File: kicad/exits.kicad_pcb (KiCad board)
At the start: 2 copper layers, 38.2 x 110 mm, 66 parts, among them IC1 NJM4556AV-TE1, IC2 NJM4556AV-TE1, J1 PJ301M12, J10 Conn_01x04_Female, J11 Conn_01x04_Male, J12 Conn_02x05_Odd_Even, J13 SJ-63083A, J14 SJ-63083A, J2 PJ301M12, J3 PJ301M12, J4 PJ301M12, J5 PJ301M12, J6 PJ301M12, J7 PJ301M12, J8 Conn_01x03_Male, J9 Conn_01x03_Female, U3 LME49720, U4 LME49720

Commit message: Add files via upload
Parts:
- J10: value Conn_01x04_Female -> Conn_01x06_Female
- J11: value Conn_01x04_Male -> Conn_01x06_Male
- J12: value Conn_02x05_Odd_Even -> Euro power header
- J8: value Conn_01x03_Male -> Conn_01x04_Male
- J9: value Conn_01x03_Female -> Conn_01x04_Female
- R11, R4: value 439k -> 442k
- R12, R3: value 103k -> 102k
- R13, R2: value 1M67 -> 1M69
- R7, R8: value 141k -> 140k
- RV1: value R_POT_Dual_Separate -> 50k A
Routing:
- net Net-(J9-Pad4): track 65.7 -> 65.1 mm
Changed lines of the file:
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@@
       (effects (font (size 1 1) (thickness 0.15)))
     )
-    (fp_text value "Conn_01x03_Male" (at 0 9.95) (layer "F.Fab")
+    (fp_text value "Conn_01x04_Male" (at 0 9.95) (layer "F.Fab")
       (effects (font (size 1 1) (thickness 0.15)))
     )
@@
       (effects (font (size 1 1) (thickness 0.15)))
     )
-    (fp_text value "Conn_01x04_Male" (at 0 15.03 90) (layer "F.Fab")
+    (fp_text value "Conn_01x06_Male" (at 0 15.03 90) (layer "F.Fab")
       (effects (font (size 1 1) (thickness 0.15)))
     )
@@
       (effects (font (size 1 1) (thickness 0.15)))
     )
-    (fp_text value "R_POT_Dual_Separate" (at 3.5 2.25 180) (layer "F.Fab") hide
+    (fp_text value "50k A" (at 3.5 2.25 180) (layer "F.Fab") hide
       (effects (font (size 1 1) (thickness 0.15)))
     )
@@
     (property "Sheetname" "")
     (attr through_hole)
-    (fp_text reference "J14" (at -4.325 -9.135 90) (layer "F.SilkS")
+    (fp_text reference "J14" (at -4.7 -6.3 90) (layer "F.SilkS")
       (effects (font (size 1 1) (thickness 0.15)))
     )
@@
     (property "Sheetname" "")
     (attr through_hole)
-    (fp_text reference "J13" (at -4.325 -9.135 90) (layer "F.SilkS")
+    (fp_text reference "J13" (at -5.4 -6.9 90) (layer "F.SilkS")
       (effects (font (size 1 1) (thickness 0.15)))
     )
@@
       (effects (font (size 0.6 0.6) (thickness 0.1)) (justify mirror))
     )
-    (fp_text value "1M67" (at 0 -1.27) (layer "B.Fab")
+    (fp_text value "1M69" (at 0 -1.27) (layer "B.Fab")
       (effects (font (size 0.6 0.6) (thickness 0.1)) (justify mirror))
     )
@@
       (effects (font (size 0.6 0.6) (thickness 0.1)) (justify mirror))
     )
-    (fp_text value "103k" (at 0 -1.27) (layer "B.Fab")
+    (fp_text value "102k" (at 0 -1.27) (layer "B.Fab")
       (effects (font (size 0.6 0.6) (thickness 0.1)) (justify mirror))
     )
@@
       (effects (font (size 0.6 0.6) (thickness 0.1)) (justify mirror))
     )
-    (fp_text value "439k" (at 0 -1.27) (layer "B.Fab")
+    (fp_text value "442k" (at 0 -1.27) (layer "B.Fab")
       (effects (font (size 0.6 0.6) (thickness 0.1)) (justify mirror))
     )
@@
       (effects (font (size 0.6 0.6) (thickness 0.1)) (justify mirror))
     )
-    (fp_text value "141k" (at 0 -1.27) (layer "B.Fab")
+    (fp_text value "140k" (at 0 -1.27) (layer "B.Fab")
       (effects (font (size 0.6 0.6) (thickness 0.1)) (justify mirror))
     )
@@
       (effects (font (size 0.6 0.6) (thickness 0.1)) (justify mirror))
     )
-    (fp_text value "141k" (at 0 -1.27) (layer "B.Fab")
+    (fp_text value "140k" (at 0 -1.27) (layer "B.Fab")
       (effects (font (size 0.6 0.6) (thickness 0.1)) (justify mirror))
     )
@@
       (effects (font (size 0.6 0.6) (thickness 0.1)) (justify mirror))
     )
-    (fp_text value "439k" (at 0 -1.27) (layer "B.Fab")
+    (fp_text value "442k" (at 0 -1.27) (layer "B.Fab")
       (effects (font (size 0.6 0.6) (thickness 0.1)) (justify mirror))
     )
@@
       (effects (font (size 0.6 0.6) (thickness 0.1)) (justify mirror))
     )
-    (fp_text value "103k" (at 0 -1.27) (layer "B.Fab")
+    (fp_text value "102k" (at 0 -1.27) (layer "B.Fab")
       (effects (font (size 0.6 0.6) (thickness 0.1)) (justify mirror))
     )
@@
       (effects (font (size 0.6 0.6) (thickness 0.1)) (justify mirror))
     )
-    (fp_text value "1M67" (at 0 -1.27) (layer "B.Fab")
+    (fp_text value "1M69" (at 0 -1.27) (layer "B.Fab")
       (effects (font (size 0.6 0.6) (thickness 0.1)) (justify mirror))
     )
@@
       (effects (font (size 1 1) (thickness 0.15)) (justify mirror))
     )
-    (fp_text value "Conn_01x03_Female" (at 0 -10.39) (layer "B.Fab")
+    (fp_text value "Conn_01x04_Female" (at 0 -10.39) (layer "B.Fab")
       (effects (font (size 1 1) (thickness 0.15)) (justify mirror))
     )
@@
       (effects (font (size 1 1) (thickness 0.15)) (justify mirror))
     )
-    (fp_text value "Conn_01x04_Female" (at 0 -15.47 90) (layer "B.Fab")
+    (fp_text value "Conn_01x06_Female" (at 0 -15.47 90) (layer "B.Fab")
       (effects (font (size 1 1) (thickness 0.15)) (justify mirror))
     )
@@
       (effects (font (size 1 1) (thickness 0.15)) (justify mirror))
     )
-    (fp_text value "Conn_02x05_Odd_Even" (at 1.27 -16.26 180) (layer "B.Fab")
+    (fp_text value "Euro power header" (at 1.27 -16.26 180) (layer "B.Fab")
       (effects (font (size 1 1) (thickness 0.15)) (justify mirror))
     )
@@
   (segment (start 134.5 78) (end 134.5 79.345) (width 0.508) (layer "F.Cu") (net 7))
   (segment (start 131 105.95) (end 129.992 105.95) (width 0.508) (layer "F.Cu") (net 7))
-  (segment (start 129.75 103.846001) (end 129.788 103.808001) (width 0.508) (layer "F.Cu") (net 7))
   (segment (start 134.5 70.595) (end 135.645 69.45) (width 0.508) (layer "F.Cu") (net 7))
   (segment (start 134.75 90.8) (end 134.75 92) (width 0.508) (layer "F.Cu") (net 7))
@@
   (segment (start 129.788 105.746) (end 129.788 103.808001) (width 0.508) (layer "F.Cu") (net 7))
   (segment (start 135.410158 45.75) (end 135.75 46.089842) (width 0.508) (layer "F.Cu") (net 7))
-  (segment (start 129.839999 103.86) (end 129.788 103.808001) (width 0.508) (layer "F.Cu") (net 7))
   (segment (start 132.15 45.65) (end 132.25 45.75) (width 0.508) (layer "F.Cu") (net 7))
   (segment (start 133.742 90.8) (end 134.75 90.8) (width 0.508) (layer "F.Cu") (net 7))
@@
   (segment (start 155.658001 108.908001) (end 155.658001 113.091999) (width 0.508) (layer "B.Cu") (net 19))
   (segment (start 154.25 107.5) (end 155.658001 108.908001) (width 0.508) (layer "B.Cu") (net 19))
-  (segment (start 155.658001 113.091999) (end 155.5 113.25) (width 0.508) (layer "B.Cu") (net 19))
   (segment (start 124.75 65.96) (end 124.75 66) (width 0.508) (layer "F.Cu") (net 21))
   (segment (start 137.75 74.55) (end 134.645 74.55) (width 0.508) (layer "F.Cu") (net 21))
@@
   (segment (start 125.941999 104.656401) (end 127.027597 105.741999) (width 0.508) (layer "F.Cu") (net 38))
   (segment (start 127.027597 105.741999) (end 128.456401 105.741999) (width 0.508) (layer "F.Cu") (net 38))
-  (segment (start 156 50.064402) (end 156 49.75) (width 0.508) (layer "B.Cu") (net 39))
   (segment (start 154.3 51.764402) (end 156 50.064402) (width 0.508) (layer "B.Cu") (net 39))
   (segment (start 156.12 49.87) (end 156 49.75) (width 0.508) (layer "B.Cu") (net 39))
@@
   (segment (start 159.55 76.95) (end 159.55 86.5) (width 0.508) (layer "B.Cu") (net 39))
   (segment (start 154.55 77.4) (end 155.41003 77.4) (width 0.508) (layer "B.Cu") (net 39))
-  (segment (start 156 49.75) (end 156.33 49.75) (width 0.508) (layer "B.Cu") (net 39))
   (segment (start 154.3 55.75) (end 154.3 60.75) (width 0.508) (layer "B.Cu") (net 39))
   (segment (start 154.3 73.5) (end 154.55 73.75) (width 0.508) (layer "B.Cu") (net 39))

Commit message: Add files via upload
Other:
- board text added: "Exits github.com/ramphands/Exits CC BY-SA 4.0"

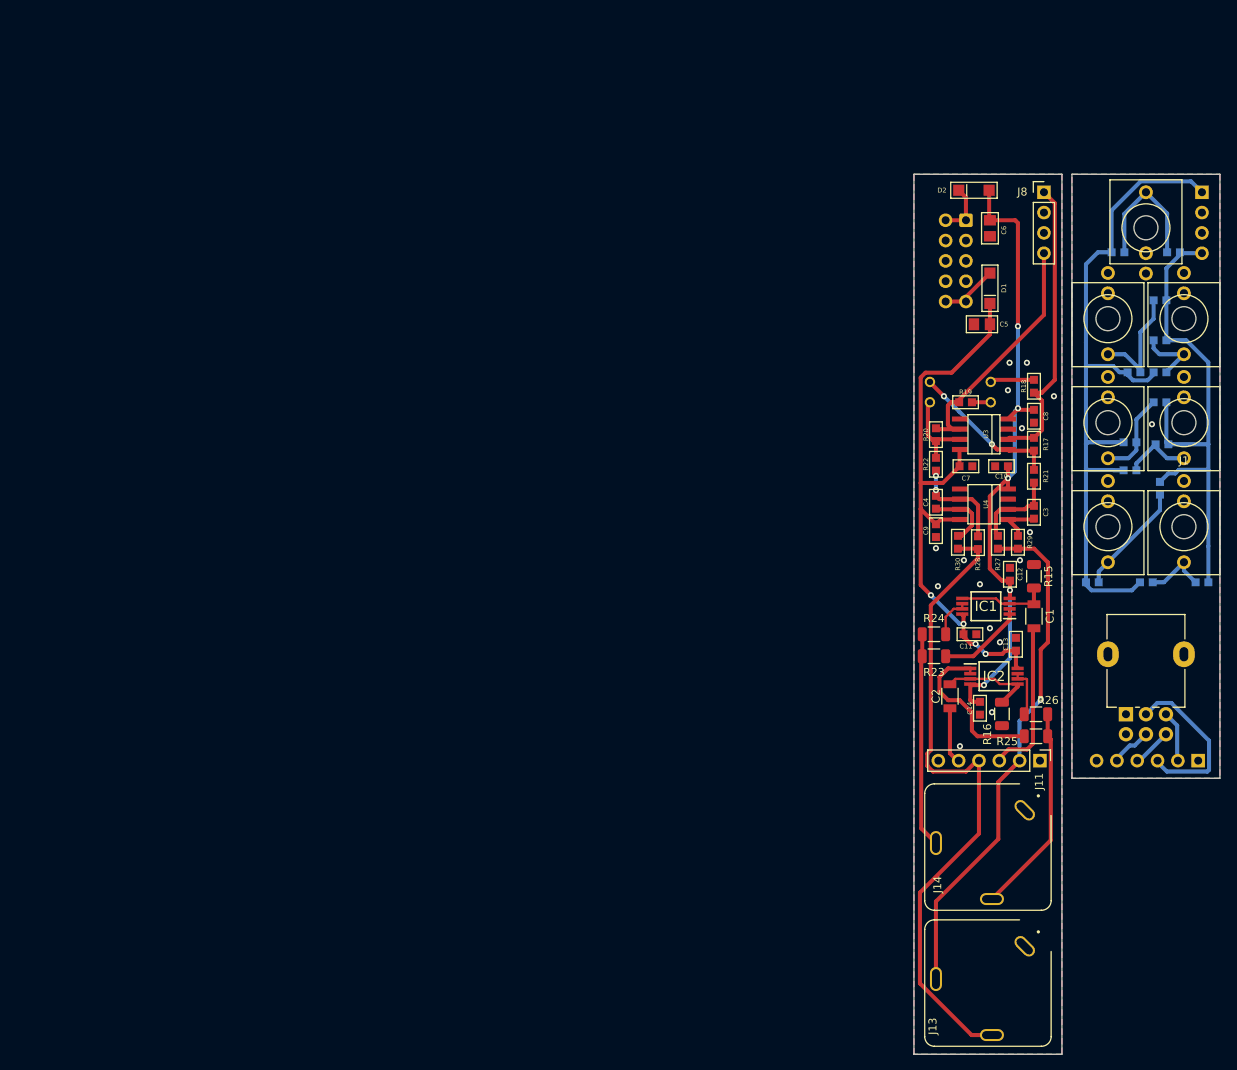
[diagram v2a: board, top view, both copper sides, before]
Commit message: Switched to CMOY style hp out w RC4850, and added stereo panning
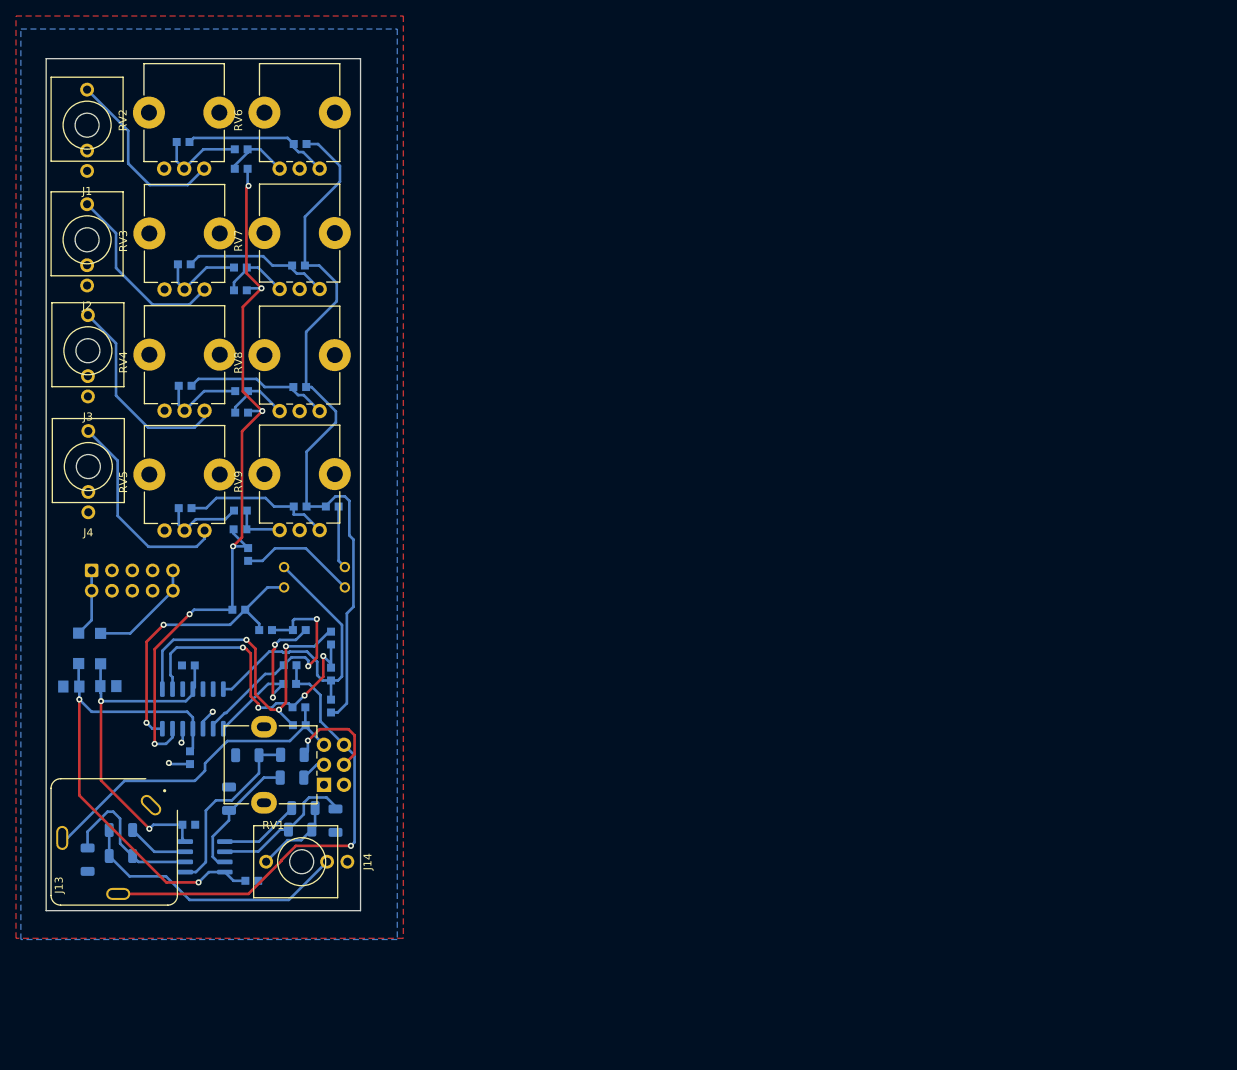
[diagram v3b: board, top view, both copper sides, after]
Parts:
- removed C11, C12, C13, C14: 100n, nearness:0603
- removed IC1, IC2: NJM4556AV-TE1, SamacSys_Parts:SOP65P640X145-8N
- removed J10: Conn_01x06_Female, Connector_PinSocket_2.54mm:PinSocket_1x06_P2.54mm_Vertical
- removed J11: Conn_01x06_Male, Connector_PinHeader_2.54mm:PinHeader_1x06_P2.54mm_Vertical
- removed J5, J6, J7: PJ301M12, nearness:PJ301M12
- removed J8: Conn_01x04_Male, Connector_PinHeader_2.54mm:PinHeader_1x04_P2.54mm_Vertical
- removed J9: Conn_01x04_Female, Connector_PinSocket_2.54mm:PinSocket_1x04_P2.54mm_Vertical
- removed U4: LME49720, nearness:SOIC-8
- added R31: R_Small, nearness:0603, B.Cu at (46.0, 81.5)
- added R32: R_Small, nearness:0603, B.Cu at (38.5, 84.4)
- added R33: 10, Resistor_SMD:R_1206_3216Metric, B.Cu at (46.4, 119.2)
- added R34: 10, Resistor_SMD:R_1206_3216Metric, B.Cu at (23.6, 122.0)
- added RV2: Volume, Potentiometer_THT:Potentiometer_Alps_RK09K_Single_Vertical, F.Cu at (34.0, 39.3)
- added RV3: Volume, Potentiometer_THT:Potentiometer_Alps_RK09K_Single_Vertical, F.Cu at (34.1, 54.4)
- added RV4: Volume, Potentiometer_THT:Potentiometer_Alps_RK09K_Single_Vertical, F.Cu at (34.1, 69.6)
- added RV5: Volume, Potentiometer_THT:Potentiometer_Alps_RK09K_Single_Vertical, F.Cu at (34.1, 84.5)
- added RV6: Pan, Potentiometer_THT:Potentiometer_Alps_RK09K_Single_Vertical, F.Cu at (48.5, 39.3)
- added RV7: Pan, Potentiometer_THT:Potentiometer_Alps_RK09K_Single_Vertical, F.Cu at (48.5, 54.4)
- added RV8: Pan, Potentiometer_THT:Potentiometer_Alps_RK09K_Single_Vertical, F.Cu at (48.5, 69.6)
- added RV9: Pan, Potentiometer_THT:Potentiometer_Alps_RK09K_Single_Vertical, F.Cu at (48.5, 84.5)
- added U2: RC4580, Package_SO:SOIC-8_3.9x4.9mm_P1.27mm, B.Cu at (34.1, 125.3)
- C1, C2: value 100n -> 0.47uF; footprint Capacitors_SMD:C_1206 -> Capacitor_SMD:C_1206_3216Metric; moved to B.Cu
- C10, C3, C4, C5, C6, C7, C8, C9, D1, D2, R15, R16, R17, R18, R19, R20, R21, R22, R27, R28, R29, R30: moved to B.Cu
- J14: value SJ-63083A -> PJ301M12; footprint Connector:CUI_SJ-63083A -> nearness:PJ301M12
- R1, R14: value 100k -> R_Small
- R10, R5: value 113k -> R_Small
- R11, R4: value 442k -> R_Small
- R12, R3: value 102k -> R_Small
- R13, R2: value 1M69 -> R_Small
- R23, R24: value 1 -> 2.2K; moved to B.Cu
- R25, R26: value 1 -> 10k; moved to B.Cu
- R6, R9: value 215k -> R_Small
- R7, R8: value 140k -> R_Small
- U1: renamed from U3; value LME49720 -> TL074; footprint nearness:SOIC-8 -> Package_SO:SOIC-14_3.9x8.7mm_P1.27mm; moved to B.Cu
- moved J1 146.0 mm to (19.4, 33.9), turned to 0 degrees
- moved J2 139.0 mm to (19.4, 48.2), turned to 0 degrees
- moved J3 137.1 mm to (19.5, 62.1), turned to 0 degrees
- moved J4 135.5 mm to (19.5, 76.5)
- moved R1 132.4 mm to (31.4, 36.0), turned to 0 degrees
- moved R2 131.7 mm to (38.7, 36.9)
- moved C6 128.3 mm to (17.4, 104.0), turned to 0 degrees
- moved D2 125.7 mm to (18.3, 99.3), turned to -90 degrees
- moved R5 121.9 mm to (31.6, 66.4), turned to 0 degrees
- moved R8 121.0 mm to (38.6, 82.0)
- moved R3 121.0 mm to (31.5, 51.3), turned to 0 degrees
- moved R7 120.9 mm to (31.6, 81.7), turned to 0 degrees
- moved D1 119.9 mm to (21.1, 99.3)
- moved C5 118.2 mm to (22.0, 104.0), turned to 0 degrees
- moved J12 117.7 mm to (20.0, 89.5), turned to -90 degrees
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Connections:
- J14 pad 3: HPoutR -> HPoutL
- R1 pad 1: Net-(J1-Pad3) -> Net-(R1-Pad1)
- R1 pad 2: Net-(J9-Pad1) -> Net-(R1-Pad2)
- R10 pad 1: Net-(J5-Pad3) -> Net-(R10-Pad1)
- R10 pad 2: Net-(J9-Pad4) -> /RightMix
- R11 pad 1: Net-(J6-Pad3) -> Net-(R11-Pad1)
- R11 pad 2: Net-(J9-Pad1) -> /LeftMix
- R12 pad 1: Net-(J6-Pad3) -> Net-(R12-Pad1)
- R12 pad 2: Net-(J9-Pad4) -> /RightMix
- R13 pad 1: Net-(J7-Pad3) -> Net-(R13-Pad1)
- R13 pad 2: Net-(J9-Pad1) -> /LeftMix
- R14 pad 1: Net-(J7-Pad3) -> Net-(R14-Pad1)
- R14 pad 2: Net-(J9-Pad4) -> /RightMix
- R17 pad 1: Net-(J8-Pad1) -> /LeftMix
- R18 pad 1: Net-(J8-Pad1) -> /LeftMix
- R19 pad 1: Net-(J8-Pad4) -> /RightMix
- R2 pad 1: Net-(J1-Pad3) -> Net-(R1-Pad1)
- R2 pad 2: Net-(J9-Pad4) -> Net-(R10-Pad1)
- R20 pad 1: Net-(J8-Pad4) -> /RightMix
- R23 pad 1: Net-(IC1-Pad1) -> GND
- R23 pad 2: HPoutL -> Net-(R23-Pad2)
- R24 pad 1: Net-(IC1-Pad6) -> GND
- R24 pad 2: HPoutL -> Net-(R24-Pad2)
- R25 pad 1: Net-(IC2-Pad1) -> HPoutL
- R25 pad 2: HPoutR -> Net-(R23-Pad2)
- R26 pad 1: Net-(IC2-Pad6) -> HPoutR
- R26 pad 2: HPoutR -> Net-(R24-Pad2)
- R3 pad 1: Net-(J2-Pad3) -> Net-(R3-Pad1)
- R3 pad 2: Net-(J9-Pad1) -> Net-(R11-Pad1)
- R4 pad 1: Net-(J2-Pad3) -> Net-(R3-Pad1)
- R4 pad 2: Net-(J9-Pad4) -> Net-(R12-Pad1)
- R5 pad 1: Net-(J3-Pad3) -> Net-(R5-Pad1)
- R5 pad 2: Net-(J9-Pad1) -> Net-(R13-Pad1)
- R6 pad 1: Net-(J3-Pad3) -> Net-(R5-Pad1)
- R6 pad 2: Net-(J9-Pad4) -> Net-(R14-Pad1)
- R7 pad 1: Net-(J4-Pad3) -> Net-(R7-Pad1)
- R7 pad 2: Net-(J9-Pad1) -> Net-(R31-Pad1)
- R8 pad 1: Net-(J4-Pad3) -> Net-(R7-Pad1)
- R8 pad 2: Net-(J9-Pad4) -> Net-(R32-Pad1)
- R9 pad 1: Net-(J5-Pad3) -> Net-(R1-Pad2)
- R9 pad 2: Net-(J9-Pad1) -> /LeftMix
- RV1 pad 1: GND -> unconnected-(RV1-Pad1)
- RV1 pad 2: Net-(J10-Pad3) -> Net-(C1-Pad1)
- RV1 pad 3: Net-(J10-Pad2) -> Lout
- RV1 pad 4: GND -> unconnected-(RV1-Pad4)
- RV1 pad 5: Net-(J10-Pad5) -> Net-(C2-Pad1)
- RV1 pad 6: Net-(J10-Pad4) -> Rout
- U1 pad 1: Net-(R17-Pad2) -> Net-(C3-Pad2)
- U1 pad 2: Net-(J8-Pad1) -> Net-(C3-Pad1)
- U1 pad 4: -12V -> +12V
- U1 pad 6: Net-(J8-Pad4) -> unconnected-(U1-Pad6)
- U1 pad 7: Net-(R20-Pad2) -> Net-(R17-Pad2)
- U1 pad 8: +12V -> Net-(C4-Pad2)
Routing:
- net /RightMix: track 0.00 -> 94.8 mm, vias 0 -> 6
- net /LeftMix: track 0.00 -> 91.8 mm
- net Net-(J9-Pad1): track 89.5 -> 0.00 mm
- net Net-(J9-Pad4): track 65.1 -> 0.00 mm
- net Net-(C3-Pad2): track 5.86 -> 44.0 mm, vias 0 -> 3
- net Net-(J8-Pad1): track 37.1 -> 0.00 mm
- net Net-(J8-Pad4): track 32.3 -> 0.00 mm
- net +12V: track 74.7 -> 44.6 mm, vias 4 -> 2
- net Net-(C3-Pad1): track 10.9 -> 39.4 mm, vias 0 -> 4
- net Net-(R20-Pad2): track 10.7 -> 35.7 mm, vias 0 -> 2
- net Rout: track 81.9 -> 58.4 mm, vias 0 -> 1
- net Lout: track 64.8 -> 42.5 mm, vias 1 -> 0
- net Net-(J10-Pad3): track 21.4 -> 0.00 mm
- net Net-(IC2-Pad1): track 21.0 -> 0.00 mm
- net -12V: track 82.1 -> 62.1 mm, vias 5 -> 2
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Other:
- board size 38.2 x 110 mm -> 39.3 x 106.5 mm
